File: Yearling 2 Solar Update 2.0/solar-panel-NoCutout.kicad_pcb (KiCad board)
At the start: 4 copper layers, 83 x 98 mm, 27 parts, among them J1 CON-5040500591, J2 Conn_01x01, J3 Conn_01x01, J4 Conn_01x01, J5 Conn_01x01, U1 APDS-9960, U2 MCP9808_DFN, U3 DRV2605LDGS

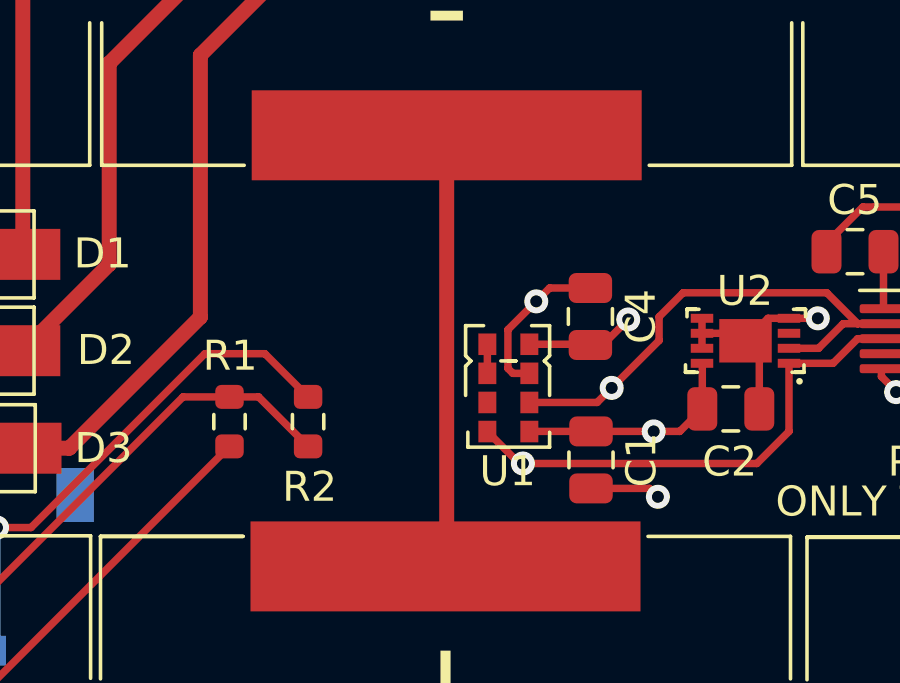
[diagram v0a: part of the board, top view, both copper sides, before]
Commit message: Minor Change to light sensor
Replaced APDS part with VLM. Also added LEDS
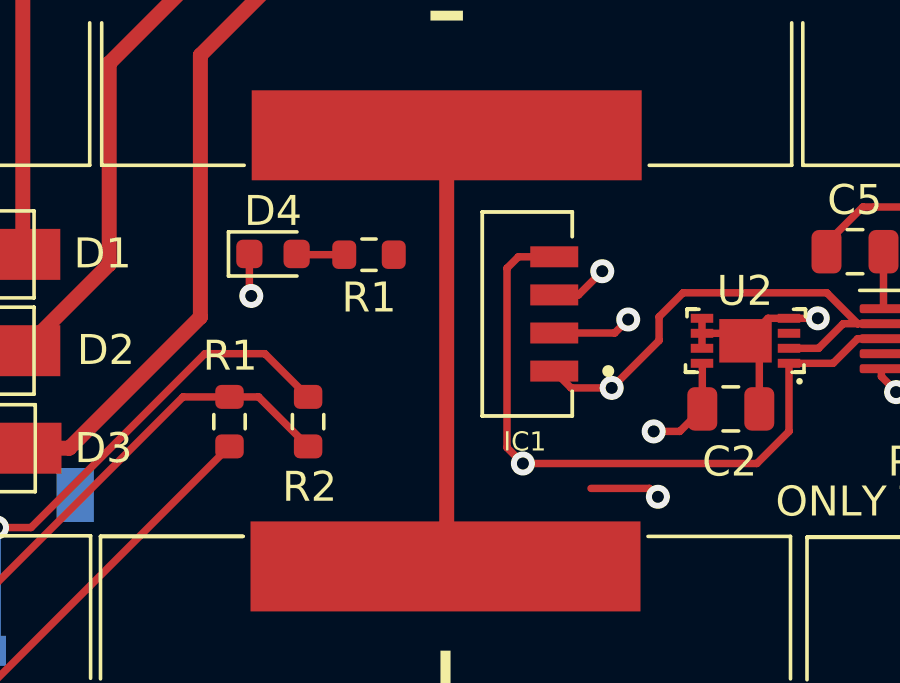
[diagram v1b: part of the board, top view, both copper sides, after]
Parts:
- removed C1, C4: 1uF, Capacitor_SMD:C_0805_2012Metric
- removed U1: APDS-9960, SolarPanelBoards:APDS-9960
- added D4: CQY99, LED_SMD:LED_0603_1608Metric, F.Cu at (138.7, 111.5)
- added IC1: VEML7700, VEML7700-TT:XDCR_VEML7700-TT, F.Cu at (147.2, 113.5)
- added R1: 1k, Resistor_SMD:R_0603_1608Metric, F.Cu at (141.9, 111.5)
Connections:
- U2 pad 6: GND -> +3V3
- U2 pad 7: GND -> +3V3
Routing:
- net SDA: track 52.5 -> 59.5 mm
- net +3V3: track 35.2 -> 30.0 mm
- net GND: track 49.9 -> 47.9 mm, vias 9 -> 10
- net Net-(R1-Pad2): track 0.00 -> 1.60 mm
- net Net-(U1-Pad3): track 0.97 -> 0.00 mm
- net SCL: track 57.1 -> 56.3 mm
